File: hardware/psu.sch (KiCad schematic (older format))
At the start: 18 parts

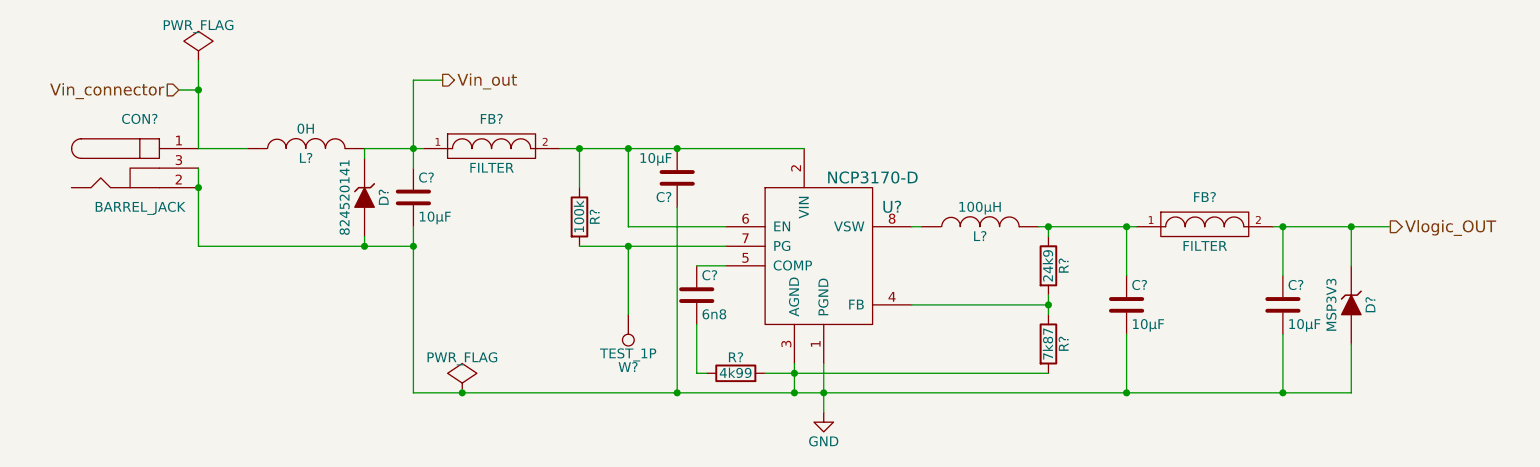
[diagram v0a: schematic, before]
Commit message: Added annotation so willing prove readers can reference components more easily
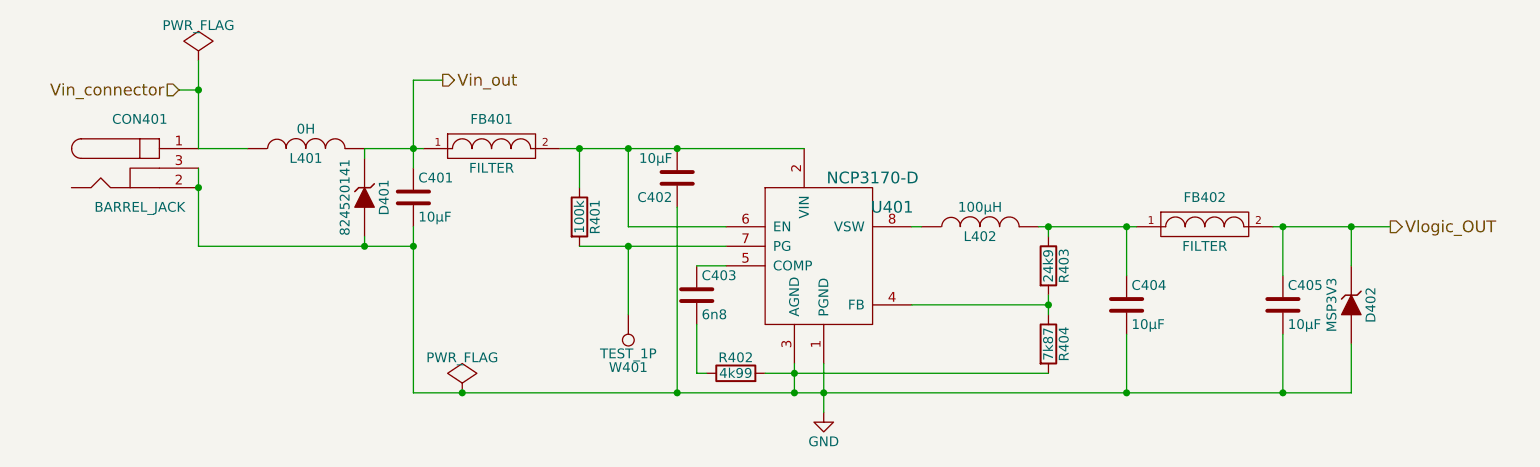
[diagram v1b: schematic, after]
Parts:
- removed C?: 10µF, symbol C
- added C401: 10µF, symbol C
- gave numbers to parts that had none: 17
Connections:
- net GND: now also C401.2
- net Vin_out: now also C401.1
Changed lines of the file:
@@
 $EndDescr
 $Comp
-L NCP3170-D U?
+L NCP3170-D U401
 U 1 1 57E31894
 P 5450 3450
-F 0 "U?" H 5800 3650 60  0000 C CNN
+F 0 "U401" H 5800 3650 60  0000 C CNN
 F 1 "NCP3170-D" H 5700 3800 60  0000 C CNN
 F 2 "" H 5450 3450 60  0001 C CNN
@@
 $EndComp
 $Comp
-L C C?
+L C C403
 U 1 1 57E318C6
 P 4800 3700
-F 0 "C?" H 4825 3800 50  0000 L CNN
+F 0 "C403" H 4825 3800 50  0000 L CNN
 F 1 "6n8" H 4825 3600 50  0000 L CNN
 F 2 "" H 4838 3550 50  0000 C CNN
@@
 $EndComp
 $Comp
-L C C?
+L C C402
 U 1 1 57E31943
 P 4700 3100
-F 0 "C?" H 4725 3200 50  0000 L CNN
+F 0 "C402" H 4725 3200 50  0000 L CNN
 F 1 "10µF" H 4725 3000 50  0000 L CNN
 F 2 "" H 4738 2950 50  0000 C CNN
@@
 $EndComp
 $Comp
-L C C?
+L C C404
 U 1 1 57E3197A
 P 7000 3750
-F 0 "C?" H 7025 3850 50  0000 L CNN
+F 0 "C404" H 7025 3850 50  0000 L CNN
 F 1 "10µF" H 7025 3650 50  0000 L CNN
 F 2 "" H 7038 3600 50  0000 C CNN
@@
 $EndComp
 $Comp
-L INDUCTOR L?
+L INDUCTOR L402
 U 1 1 57E319E7
 P 6250 3350
-F 0 "L?" V 6200 3350 50  0000 C CNN
+F 0 "L402" V 6200 3350 50  0000 C CNN
 F 1 "100µH" V 6350 3350 50  0000 C CNN
 F 2 "" H 6250 3350 50  0000 C CNN
@@
 $EndComp
 $Comp
-L R R?
+L R R403
 U 1 1 57E31B20
 P 6600 3550
-F 0 "R?" V 6680 3550 50  0000 C CNN
+F 0 "R403" V 6680 3550 50  0000 C CNN
 F 1 "24k9" V 6600 3550 50  0000 C CNN
 F 2 "" V 6530 3550 50  0000 C CNN
@@
 $EndComp
 $Comp
-L R R?
+L R R404
 U 1 1 57E31B73
 P 6600 3950
-F 0 "R?" V 6680 3950 50  0000 C CNN
+F 0 "R404" V 6680 3950 50  0000 C CNN
 F 1 "7k87" V 6600 3950 50  0000 C CNN
 F 2 "" V 6530 3950 50  0000 C CNN
@@
 $EndComp
 $Comp
-L R R?
+L R R402
 U 1 1 57E31B96
 P 5000 4100
-F 0 "R?" V 5080 4100 50  0000 C CNN
+F 0 "R402" V 5080 4100 50  0000 C CNN
 F 1 "4k99" V 5000 4100 50  0000 C CNN
 F 2 "" V 4930 4100 50  0000 C CNN
@@
 Connection ~ 5450 4200
 $Comp
-L GND #PWR014
+L GND #PWR401
 U 1 1 57E32388
 P 5450 4300
-F 0 "#PWR014" H 5450 4050 50  0001 C CNN
+F 0 "#PWR401" H 5450 4050 50  0001 C CNN
 F 1 "GND" H 5450 4150 50  0000 C CNN
 F 2 "" H 5450 4300 50  0000 C CNN
@@
 $EndComp
 $Comp
-L BARREL_JACK CON?
+L BARREL_JACK CON401
 U 1 1 57E323EC
 P 1950 3050
-F 0 "CON?" H 1950 3300 50  0000 C CNN
+F 0 "CON401" H 1950 3300 50  0000 C CNN
 F 1 "BARREL_JACK" H 1950 2850 50  0000 C CNN
 F 2 "" H 1950 3050 50  0000 C CNN
@@
 Connection ~ 7000 3350
 $Comp
-L TEST_1P W?
+L TEST_1P W401
 U 1 1 57E328A9
 P 4450 3800
-F 0 "W?" H 4450 4070 50  0000 C CNN
+F 0 "W401" H 4450 4070 50  0000 C CNN
 F 1 "TEST_1P" H 4450 4000 50  0000 C CNN
 F 2 "" H 4650 3800 50  0000 C CNN
@@
 	4200 3450 4950 3450
 $Comp
-L C C?
-U 1 1 57E32ACD
+L C C401
+U 1 1 57ECEA95
 P 3350 3200
-F 0 "C?" H 3375 3300 50  0000 L CNN
+F 0 "C401" H 3375 3300 50  0000 L CNN
 F 1 "10µF" H 3375 3100 50  0000 L CNN
 F 2 "" H 3388 3050 50  0000 C CNN
@@
 Connection ~ 4700 4200
 $Comp
-L C C?
+L C C405
 U 1 1 57E32EF4
 P 7800 3750
-F 0 "C?" H 7825 3850 50  0000 L CNN
+F 0 "C405" H 7825 3850 50  0000 L CNN
 F 1 "10µF" H 7825 3650 50  0000 L CNN
 F 2 "" H 7838 3600 50  0000 C CNN
@@
 Vlogic_OUT
 $Comp
-L PWR_FLAG #FLG015
+L PWR_FLAG #FLG402
 U 1 1 57E33511
 P 3600 4200
-F 0 "#FLG015" H 3600 4295 50  0001 C CNN
+F 0 "#FLG402" H 3600 4295 50  0001 C CNN
 F 1 "PWR_FLAG" H 3600 4380 50  0000 C CNN
 F 2 "" H 3600 4200 50  0000 C CNN
@@
 	5150 4100 6600 4100
 $Comp
-L R R?
+L R R401
 U 1 1 57E40BA6
 P 4200 3300
-F 0 "R?" V 4280 3300 50  0000 C CNN
+F 0 "R401" V 4280 3300 50  0000 C CNN
 F 1 "100k" V 4200 3300 50  0000 C CNN
 F 2 "" V 4130 3300 50  0000 C CNN
@@
 Connection ~ 3350 2950
 $Comp
-L PWR_FLAG #FLG016
+L PWR_FLAG #FLG401
 U 1 1 57E44620
 P 2250 2500
-F 0 "#FLG016" H 2250 2595 50  0001 C CNN
+F 0 "#FLG401" H 2250 2595 50  0001 C CNN
 F 1 "PWR_FLAG" H 2250 2680 50  0000 C CNN
 F 2 "" H 2250 2500 50  0000 C CNN
@@
 	2250 2500 2250 2950
 $Comp
-L INDUCTOR L?
+L INDUCTOR L401
 U 1 1 57E56F10
 P 2800 2950
-F 0 "L?" V 2750 2950 50  0000 C CNN
+F 0 "L401" V 2750 2950 50  0000 C CNN
 F 1 "0H" V 2900 2950 50  0000 C CNN
 F 2 "" H 2800 2950 50  0000 C CNN
@@
 	3350 2600 3350 3050
 $Comp
-L ZENER D?
+L ZENER D401
 U 1 1 57E57556
 P 3100 3200
-F 0 "D?" H 3100 3300 50  0000 C CNN
+F 0 "D401" H 3100 3300 50  0000 C CNN
 F 1 "824520141" H 3100 3100 50  0000 C CNN
 F 2 "" H 3100 3200 50  0000 C CNN
@@
 	3500 2600 3350 2600
 $Comp
-L FILTER FB?
+L FILTER FB401
 U 1 1 57E5F407
 P 3750 2950
-F 0 "FB?" H 3750 3100 50  0000 C CNN
+F 0 "FB401" H 3750 3100 50  0000 C CNN
 F 1 "FILTER" H 3750 2850 50  0000 C CNN
 F 2 "" H 3750 2950 50  0000 C CNN
@@
 $EndComp
 $Comp
-L FILTER FB?
+L FILTER FB402
 U 1 1 57E5F6B8
 P 7400 3350
-F 0 "FB?" H 7400 3500 50  0000 C CNN
+F 0 "FB402" H 7400 3500 50  0000 C CNN
 F 1 "FILTER" H 7400 3250 50  0000 C CNN
 F 2 "" H 7400 3350 50  0000 C CNN
@@
 	6550 3350 7050 3350
 $Comp
-L ZENER D?
+L ZENER D402
 U 1 1 57ED7CD8
 P 8150 3750
-F 0 "D?" H 8150 3850 50  0000 C CNN
+F 0 "D402" H 8150 3850 50  0000 C CNN
 F 1 "MSP3V3" H 8150 3650 50  0000 C CNN
 F 2 "" H 8150 3750 50  0000 C CNN

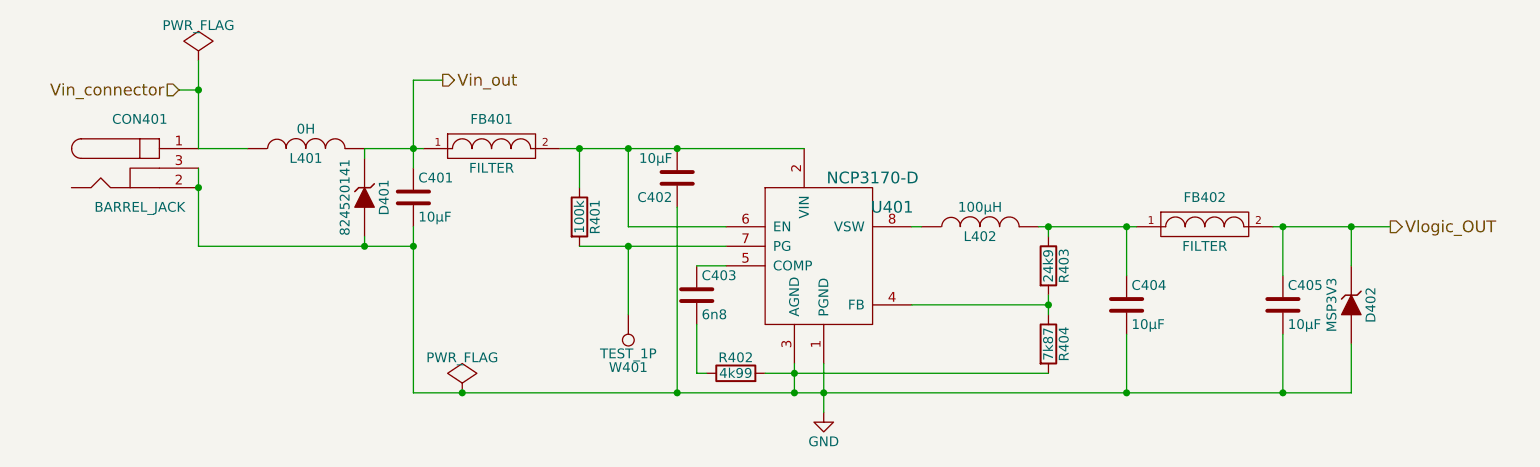
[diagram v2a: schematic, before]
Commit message: fixed some more ERC errors
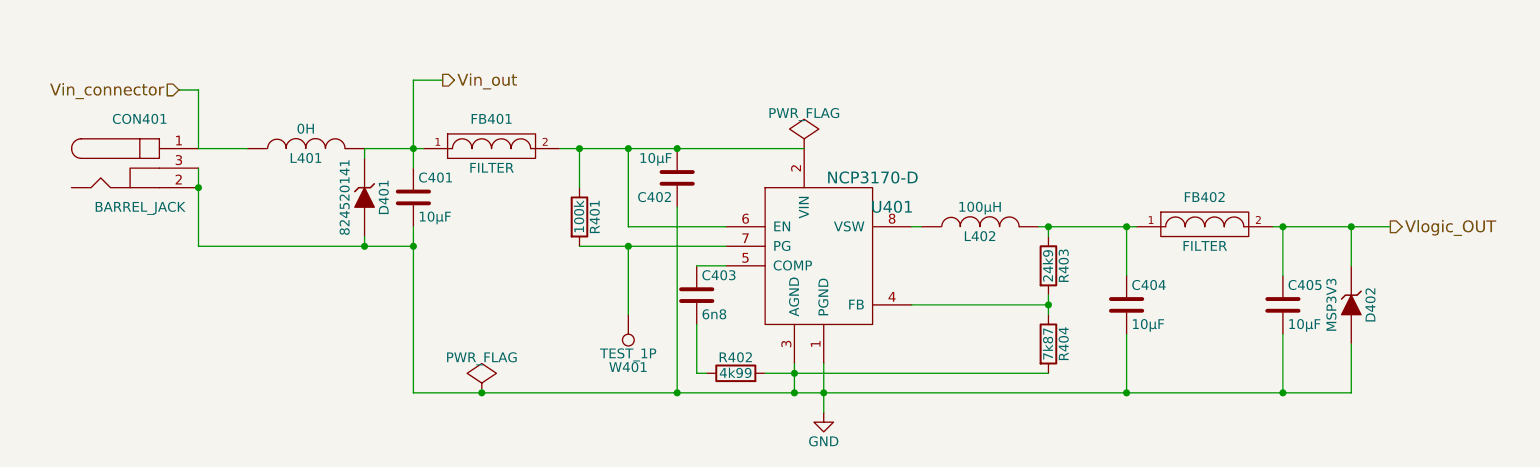
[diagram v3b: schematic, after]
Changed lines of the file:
@@
 Connection ~ 5450 4200
 $Comp
-L GND #PWR015
+L GND #PWR018
 U 1 1 57E32388
 P 5450 4300
-F 0 "#PWR015" H 5450 4050 50  0001 C CNN
+F 0 "#PWR018" H 5450 4050 50  0001 C CNN
 F 1 "GND" H 5450 4150 50  0000 C CNN
 F 2 "" H 5450 4300 50  0000 C CNN
@@
 Text HLabel 8350 3350 2    60   Output ~ 0
 Vlogic_OUT
-$Comp
-L PWR_FLAG #FLG016
-U 1 1 57E33511
-P 3600 4200
-F 0 "#FLG016" H 3600 4295 50  0001 C CNN
-F 1 "PWR_FLAG" H 3600 4380 50  0000 C CNN
-F 2 "" H 3600 4200 50  0000 C CNN
-F 3 "" H 3600 4200 50  0000 C CNN
-	1    3600 4200
-	1    0    0    -1
-$EndComp
 Wire Wire Line
 	5150 4100 6600 4100
@@
 Connection ~ 4200 2950
 Connection ~ 4450 3450
-Connection ~ 3600 4200
 Connection ~ 3350 2950
 $Comp
-L PWR_FLAG #FLG017
+L PWR_FLAG #FLG019
 U 1 1 57E44620
-P 2250 2500
-F 0 "#FLG017" H 2250 2595 50  0001 C CNN
-F 1 "PWR_FLAG" H 2250 2680 50  0000 C CNN
-F 2 "" H 2250 2500 50  0000 C CNN
-F 3 "" H 2250 2500 50  0000 C CNN
-	1    2250 2500
+P 5350 2950
+F 0 "#FLG019" H 5350 3045 50  0001 C CNN
+F 1 "PWR_FLAG" H 5350 3130 50  0000 C CNN
+F 2 "" H 5350 2950 50  0000 C CNN
+F 3 "" H 5350 2950 50  0000 C CNN
+	1    5350 2950
 	1    0    0    -1
 $EndComp
@@
 Wire Wire Line
 	2150 2650 2250 2650
-Wire Wire Line
-	2250 2500 2250 2950
 $Comp
 L INDUCTOR L401
@@
 Wire Wire Line
 	3100 2950 3400 2950
-Connection ~ 2250 2650
 Wire Wire Line
 	3350 2600 3350 3050
@@
 Wire Wire Line
 	7000 3900 7000 4200
+Wire Wire Line
+	2250 2650 2250 2950
+$Comp
+L PWR_FLAG #FLG020
+U 1 1 57EE5195
+P 3700 4200
+F 0 "#FLG020" H 3700 4295 50  0001 C CNN
+F 1 "PWR_FLAG" H 3700 4380 50  0000 C CNN
+F 2 "" H 3700 4200 50  0000 C CNN
+F 3 "" H 3700 4200 50  0000 C CNN
+	1    3700 4200
+	1    0    0    -1
+$EndComp
+Connection ~ 3700 4200
 $EndSCHEMATC

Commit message: Linked first components to footprints and updated schematic plot
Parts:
- C401, C402, C403, C404, C405: footprint (none) -> Capacitors_SMD:C_0805
- D401: footprint (none) -> Diodes_SMD:SMA_Handsoldering
- R401, R402, R403, R404: footprint (none) -> Resistors_SMD:R_0805_HandSoldering
- W401: footprint (none) -> Measurement_Points:Measurement_Point_Round-SMD-Pad_Big
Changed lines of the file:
@@
 F 0 "C403" H 4825 3800 50  0000 L CNN
 F 1 "6n8" H 4825 3600 50  0000 L CNN
-F 2 "" H 4838 3550 50  0000 C CNN
+F 2 "Capacitors_SMD:C_0805" H 4838 3550 50  0001 C CNN
 F 3 "" H 4800 3700 50  0000 C CNN
 	1    4800 3700
@@
 F 0 "C402" H 4725 3200 50  0000 L CNN
 F 1 "10µF" H 4725 3000 50  0000 L CNN
-F 2 "" H 4738 2950 50  0000 C CNN
+F 2 "Capacitors_SMD:C_0805" H 4738 2950 50  0001 C CNN
 F 3 "" H 4700 3100 50  0000 C CNN
 	1    4700 3100
@@
 F 0 "C404" H 7025 3850 50  0000 L CNN
 F 1 "10µF" H 7025 3650 50  0000 L CNN
-F 2 "" H 7038 3600 50  0000 C CNN
+F 2 "Capacitors_SMD:C_0805" H 7038 3600 50  0001 C CNN
 F 3 "" H 7000 3750 50  0000 C CNN
 	1    7000 3750
@@
 F 0 "L402" V 6200 3350 50  0000 C CNN
 F 1 "100µH" V 6350 3350 50  0000 C CNN
-F 2 "" H 6250 3350 50  0000 C CNN
+F 2 "" H 6250 3350 50  0001 C CNN
 F 3 "" H 6250 3350 50  0000 C CNN
 	1    6250 3350
@@
 F 0 "R403" V 6680 3550 50  0000 C CNN
 F 1 "24k9" V 6600 3550 50  0000 C CNN
-F 2 "" V 6530 3550 50  0000 C CNN
+F 2 "Resistors_SMD:R_0805_HandSoldering" V 6530 3550 50  0001 C CNN
 F 3 "" H 6600 3550 50  0000 C CNN
 	1    6600 3550
@@
 F 0 "R404" V 6680 3950 50  0000 C CNN
 F 1 "7k87" V 6600 3950 50  0000 C CNN
-F 2 "" V 6530 3950 50  0000 C CNN
+F 2 "Resistors_SMD:R_0805_HandSoldering" V 6530 3950 50  0001 C CNN
 F 3 "" H 6600 3950 50  0000 C CNN
 	1    6600 3950
@@
 F 0 "R402" V 5080 4100 50  0000 C CNN
 F 1 "4k99" V 5000 4100 50  0000 C CNN
-F 2 "" V 4930 4100 50  0000 C CNN
+F 2 "Resistors_SMD:R_0805_HandSoldering" V 4930 4100 50  0001 C CNN
 F 3 "" H 5000 4100 50  0000 C CNN
 	1    5000 4100
@@
 Connection ~ 5450 4200
 $Comp
-L GND #PWR401
+L GND #PWR018
 U 1 1 57E32388
 P 5450 4300
-F 0 "#PWR401" H 5450 4050 50  0001 C CNN
+F 0 "#PWR018" H 5450 4050 50  0001 C CNN
 F 1 "GND" H 5450 4150 50  0000 C CNN
 F 2 "" H 5450 4300 50  0000 C CNN
@@
 F 0 "CON401" H 1950 3300 50  0000 C CNN
 F 1 "BARREL_JACK" H 1950 2850 50  0000 C CNN
-F 2 "" H 1950 3050 50  0000 C CNN
+F 2 "" H 1950 3050 50  0001 C CNN
 F 3 "" H 1950 3050 50  0000 C CNN
 	1    1950 3050
@@
 F 0 "W401" H 4450 4070 50  0000 C CNN
 F 1 "TEST_1P" H 4450 4000 50  0000 C CNN
-F 2 "" H 4650 3800 50  0000 C CNN
+F 2 "Measurement_Points:Measurement_Point_Round-SMD-Pad_Big" H 4650 3800 50  0001 C CNN
 F 3 "" H 4650 3800 50  0000 C CNN
 	1    4450 3800
@@
 F 0 "C401" H 3375 3300 50  0000 L CNN
 F 1 "10µF" H 3375 3100 50  0000 L CNN
-F 2 "" H 3388 3050 50  0000 C CNN
+F 2 "Capacitors_SMD:C_0805" H 3388 3050 50  0001 C CNN
 F 3 "" H 3350 3200 50  0000 C CNN
 	1    3350 3200
@@
 F 0 "C405" H 7825 3850 50  0000 L CNN
 F 1 "10µF" H 7825 3650 50  0000 L CNN
-F 2 "" H 7838 3600 50  0000 C CNN
+F 2 "Capacitors_SMD:C_0805" H 7838 3600 50  0001 C CNN
 F 3 "" H 7800 3750 50  0000 C CNN
 	1    7800 3750
@@
 F 0 "R401" V 4280 3300 50  0000 C CNN
 F 1 "100k" V 4200 3300 50  0000 C CNN
-F 2 "" V 4130 3300 50  0000 C CNN
+F 2 "Resistors_SMD:R_0805_HandSoldering" V 4130 3300 50  0001 C CNN
 F 3 "" H 4200 3300 50  0000 C CNN
 	1    4200 3300
@@
 Connection ~ 3350 2950
 $Comp
-L PWR_FLAG #FLG402
+L PWR_FLAG #FLG019
 U 1 1 57E44620
 P 5350 2950
-F 0 "#FLG402" H 5350 3045 50  0001 C CNN
+F 0 "#FLG019" H 5350 3045 50  0001 C CNN
 F 1 "PWR_FLAG" H 5350 3130 50  0000 C CNN
 F 2 "" H 5350 2950 50  0000 C CNN
@@
 F 0 "L401" V 2750 2950 50  0000 C CNN
 F 1 "0H" V 2900 2950 50  0000 C CNN
-F 2 "" H 2800 2950 50  0000 C CNN
+F 2 "" H 2800 2950 50  0001 C CNN
 F 3 "" H 2800 2950 50  0000 C CNN
 	1    2800 2950
@@
 F 0 "D401" H 3100 3300 50  0000 C CNN
 F 1 "824520141" H 3100 3100 50  0000 C CNN
-F 2 "" H 3100 3200 50  0000 C CNN
+F 2 "Diodes_SMD:SMA_Handsoldering" H 3100 3200 50  0001 C CNN
 F 3 "" H 3100 3200 50  0000 C CNN
 	1    3100 3200
@@
 F 0 "FB401" H 3750 3100 50  0000 C CNN
 F 1 "FILTER" H 3750 2850 50  0000 C CNN
-F 2 "" H 3750 2950 50  0000 C CNN
+F 2 "" H 3750 2950 50  0001 C CNN
 F 3 "" H 3750 2950 50  0000 C CNN
 	1    3750 2950
@@
 F 0 "FB402" H 7400 3500 50  0000 C CNN
 F 1 "FILTER" H 7400 3250 50  0000 C CNN
-F 2 "" H 7400 3350 50  0000 C CNN
+F 2 "" H 7400 3350 50  0001 C CNN
 F 3 "" H 7400 3350 50  0000 C CNN
 	1    7400 3350
@@
 F 0 "D402" H 8150 3850 50  0000 C CNN
 F 1 "MSP3V3" H 8150 3650 50  0000 C CNN
-F 2 "" H 8150 3750 50  0000 C CNN
+F 2 "" H 8150 3750 50  0001 C CNN
 F 3 "" H 8150 3750 50  0000 C CNN
 	1    8150 3750
@@
 	2250 2650 2250 2950
 $Comp
-L PWR_FLAG #FLG401
+L PWR_FLAG #FLG020
 U 1 1 57EE5195
 P 3700 4200
-F 0 "#FLG401" H 3700 4295 50  0001 C CNN
+F 0 "#FLG020" H 3700 4295 50  0001 C CNN
 F 1 "PWR_FLAG" H 3700 4380 50  0000 C CNN
 F 2 "" H 3700 4200 50  0000 C CNN
